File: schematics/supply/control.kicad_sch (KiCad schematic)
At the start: 66 parts, among them J10 USBASP, J11 USBASP, J12 Conn_01x06_Pin, J13 Conn_01x06_Pin, J6 Conn_01x04_Pin, J7 Conn_01x04_Pin, J8 Conn_01x04_Pin, J9 Conn_01x04_Pin, M1 Fan, Q10 IRLML5203, Q4 IRLML0030, Q7 IRLML0030, SW1 EC11W****, SW3 SW_Push, U12 ATmega328-A, U13 ATtiny1616-M, U14 Display_2.2inch_ili9341, U15 LM158DR, X1 HC-49U, 16MHz, X2 CSX-750FCC, 16MHz

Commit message: Found and fixed issues in schematics.
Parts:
- X2: value CSX-750FCC, 16MHz -> 16MHz, SMD3225
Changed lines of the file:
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@@
       (effects (font (size 1.27 1.27)))
     )
-    (property "Value" "CSX-750FCC, 16MHz" (at 213.36 304.8 0)
+    (property "Value" "16MHz, SMD3225" (at 213.36 304.8 0)
       (effects (font (size 1.27 1.27)))
     )

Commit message: Some changes
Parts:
- C21: value 100 nF -> 1 uF
- C26, C29, C35, C36, C37: value 100 nF -> 220 nF
- C36: value 1 uF -> 220 nF
- R30: value 100K -> 10K
- R32: value 200K -> 10K
- R35, R36: value 5K -> 5K1
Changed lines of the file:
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@@
   (symbol (lib_id "Device:C") (at 415.29 389.89 180) (unit 1)
     (in_bom yes) (on_board yes) (dnp no) (fields_autoplaced)
-    (property "Reference" "C36" (at 419.1 389.255 0)
-      (effects (font (size 1.27 1.27)) (justify right))
-    )
-    (property "Value" "1 uF" (at 419.1 391.795 0)
+    (property "Reference" "C36" (at 419.1 388.62 0)
+      (effects (font (size 1.27 1.27)) (justify right))
+    )
+    (property "Value" "220 nF" (at 419.1 391.16 0)
       (effects (font (size 1.27 1.27)) (justify right))
     )
@@
       (effects (font (size 1.27 1.27)))
     )
-    (property "Value" "100 nF" (at 77.47 165.1 90)
+    (property "Value" "220 nF" (at 77.47 165.1 90)
       (effects (font (size 1.27 1.27)))
     )
@@
       (effects (font (size 1.27 1.27) italic) hide)
     )
-    (property "Datasheet" "http://ww1.microchip.com/downloads/en/DeviceDoc/ATtiny3216_ATtiny1616-data-sheet-40001997B.pdf" (at 101.6 331.47 0)
+    (property "Datasheet" "https://static.chipdip.ru/lib/430/DOC011430662.pdf" (at 101.6 331.47 0)
       (effects (font (size 1.27 1.27)) hide)
     )
@@
   (symbol (lib_id "Device:R") (at 208.28 88.9 180) (unit 1)
     (in_bom yes) (on_board yes) (dnp no) (fields_autoplaced)
-    (property "Reference" "R30" (at 210.82 88.265 0)
-      (effects (font (size 1.27 1.27)) (justify right))
-    )
-    (property "Value" "100K" (at 210.82 90.805 0)
+    (property "Reference" "R30" (at 210.82 87.63 0)
+      (effects (font (size 1.27 1.27)) (justify right))
+    )
+    (property "Value" "10K" (at 210.82 90.17 0)
       (effects (font (size 1.27 1.27)) (justify right))
     )
@@
   (symbol (lib_id "Device:C") (at 396.24 369.57 180) (unit 1)
     (in_bom yes) (on_board yes) (dnp no) (fields_autoplaced)
-    (property "Reference" "C36" (at 400.05 368.935 0)
-      (effects (font (size 1.27 1.27)) (justify right))
-    )
-    (property "Value" "1 uF" (at 400.05 371.475 0)
+    (property "Reference" "C36" (at 400.05 368.3 0)
+      (effects (font (size 1.27 1.27)) (justify right))
+    )
+    (property "Value" "220 nF" (at 400.05 370.84 0)
       (effects (font (size 1.27 1.27)) (justify right))
     )
@@
       (effects (font (size 1.27 1.27)) hide)
     )
-    (property "Value" "100 nF" (at 171.45 165.1 90)
+    (property "Value" "220 nF" (at 171.45 165.1 90)
       (effects (font (size 1.27 1.27)))
     )
@@
       (effects (font (size 1.27 1.27)) (justify right))
     )
-    (property "Value" "5K" (at 388.62 370.84 0)
+    (property "Value" "5K1" (at 388.62 370.84 0)
       (effects (font (size 1.27 1.27)) (justify right))
     )
@@
   (symbol (lib_id "Device:C") (at 396.24 294.64 180) (unit 1)
     (in_bom yes) (on_board yes) (dnp no) (fields_autoplaced)
-    (property "Reference" "C36" (at 400.05 294.005 0)
-      (effects (font (size 1.27 1.27)) (justify right))
-    )
-    (property "Value" "1 uF" (at 400.05 296.545 0)
+    (property "Reference" "C36" (at 400.05 293.37 0)
+      (effects (font (size 1.27 1.27)) (justify right))
+    )
+    (property "Value" "220 nF" (at 400.05 295.91 0)
       (effects (font (size 1.27 1.27)) (justify right))
     )
@@
       (effects (font (size 1.27 1.27)))
     )
-    (property "Value" "100 nF" (at 77.47 179.07 90)
+    (property "Value" "220 nF" (at 77.47 179.07 90)
       (effects (font (size 1.27 1.27)))
     )
@@
       (effects (font (size 1.27 1.27)))
     )
-    (property "Value" "100 nF" (at 171.45 191.77 90)
+    (property "Value" "220 nF" (at 171.45 191.77 90)
       (effects (font (size 1.27 1.27)))
     )
@@
       (effects (font (size 1.27 1.27)) (justify right))
     )
-    (property "Value" "200K" (at 262.89 31.75 0)
+    (property "Value" "10K" (at 262.89 31.75 0)
       (effects (font (size 1.27 1.27)) (justify right))
     )
@@
       (effects (font (size 1.27 1.27)))
     )
-    (property "Value" "100 nF" (at 77.47 191.77 90)
+    (property "Value" "220 nF" (at 77.47 191.77 90)
       (effects (font (size 1.27 1.27)))
     )
@@
       (effects (font (size 1.27 1.27)) (justify left))
     )
-    (property "Value" "100 nF" (at 127 295.91 0)
+    (property "Value" "220 nF" (at 127 295.91 0)
       (effects (font (size 1.27 1.27)) (justify left))
     )
@@
       (effects (font (size 1.27 1.27)) (justify left))
     )
-    (property "Value" "100 nF" (at 33.02 52.07 0)
+    (property "Value" "1 uF" (at 33.02 52.07 0)
       (effects (font (size 1.27 1.27)) (justify left))
     )
@@
       (effects (font (size 1.27 1.27)) (justify right))
     )
-    (property "Value" "5K" (at 388.62 295.91 0)
+    (property "Value" "5K1" (at 388.62 295.91 0)
       (effects (font (size 1.27 1.27)) (justify right))
     )
@@
       (effects (font (size 1.27 1.27)) (justify left))
     )
-    (property "Value" "100 nF" (at 121.92 81.28 0)
+    (property "Value" "220 nF" (at 121.92 81.28 0)
       (effects (font (size 1.27 1.27)) (justify left))
     )
@@
       (effects (font (size 1.27 1.27)))
     )
-    (property "Value" "100 nF" (at 171.45 179.07 90)
+    (property "Value" "220 nF" (at 171.45 179.07 90)
       (effects (font (size 1.27 1.27)))
     )
@@
   (symbol (lib_id "Device:C") (at 415.29 314.96 180) (unit 1)
     (in_bom yes) (on_board yes) (dnp no) (fields_autoplaced)
-    (property "Reference" "C36" (at 419.1 314.325 0)
-      (effects (font (size 1.27 1.27)) (justify right))
-    )
-    (property "Value" "1 uF" (at 419.1 316.865 0)
-      (effects (font (size 1.27 1.27)) (justify right))
-    )
+    (property "Reference" "C36" (at 419.1 313.69 0)
+      (effects (font (size 1.27 1.27)) (justify right))
+    )
+    (property "Value" "220 nF" (at 419.1 316.23 0)
+      (effects (font (size 1.27 1.27)) (justify right))
+    )

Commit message: fix pins in firmware
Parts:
- added J23: Conn_01x06_Pin, symbol Connector:Conn_01x06_Pin
- added U22: Display_1.18inch_st7535, symbol My_Library:Display_1.18inch_st7535
- J7, J9, SW1: now fitted; now in the parts list
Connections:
- new net: J23.1 (Pin_1), U22.11 (VCC), U22.2 (RESET)
- new net: J23.2 (Pin_2), U22.3 (DC)
- new net: J23.3 (Pin_3), U22.4 (MOSI)
- new net: J23.4 (Pin_4), U22.5 (SCK)
- new net: J23.6 (Pin_6), U22.1 (CS), U22.10 (GND), U22.9 (GND)
- no-connect marks 9 -> 10

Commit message: supply board - power controllers changed; PWM logic changed
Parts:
- removed C30: 100 nF, Capacitor_SMD:C_0603_1608Metric, symbol Device:C
- removed D14: BAV21WS, Diode_SMD:D_SOD-323F, symbol Device:D
- removed J11: USBASP, Connector_PinHeader_2.54mm:PinHeader_2x05_P2.54mm_Vertical, symbol Connector_Generic:Conn_02x05_Odd_Even
- removed J13: Conn_01x06_Pin, symbol Connector:Conn_01x06_Pin
- removed JP4: Jumper_2_Open, TestPoint:TestPoint_2Pads_Pitch2.54mm_Drill0.8mm, symbol Jumper:Jumper_2_Open
- removed Q10: IRLML5203, Package_TO_SOT_SMD:SOT-23, symbol Transistor_FET:IRLML5203
- removed R37: 10K, Resistor_SMD:R_0805_2012Metric, symbol Device:R
- removed U14: Display_2.2inch_ili9341, symbol My_Library:Display_2.2inch_ili9341
- removed X2: 16MHz, SMD3225, Oscillator:Oscillator_SMD_Abracon_ASE-4Pin_3.2x2.5mm, symbol Oscillator:SG-211
- added C36: 100 nF, Capacitor_SMD:C_0603_1608Metric, symbol Device:C
- added C36: 10 nF, Capacitor_SMD:C_0603_1608Metric, symbol Device:C
- added C41, C43, C47, C51: 1 uF, Capacitor_SMD:C_0603_1608Metric, symbol Device:C
- added D18: BAV21WS, Diode_SMD:D_SOD-323F, symbol Device:D
- added D22: GNL-3012GD, Connector_JST:JST_XH_B2B-XH-A_1x02_P2.50mm_Vertical, symbol Device:LED
- added J12: JST XH B3B, Connector_JST:JST_XH_B3B-XH-A_1x03_P2.50mm_Vertical, symbol Connector:Conn_01x03_Socket
- added J14: Conn_01x03_Pin, symbol Connector:Conn_01x03_Pin
- added J25: Conn_01x05_Socket, Connector_PinHeader_2.54mm:PinHeader_1x05_P2.54mm_Vertical, symbol Connector:Conn_01x05_Socket
- added Q4: IRLML0030, Package_TO_SOT_SMD:SOT-23, symbol Transistor_FET:IRLML0030
- added R35: 10K, Resistor_SMD:R_0805_2012Metric, symbol Device:R
- added R36: 270, Resistor_SMD:R_0805_2012Metric, symbol Device:R
- added R40: 1K, Resistor_SMD:R_0805_2012Metric, symbol Device:R
- added U17: AD9833xRM, Package_SO:MSOP-10_3x3mm_P0.5mm, symbol Interface:AD9833xRM
- added U18: MCP4726A0T-E/CH, Package_TO_SOT_SMD:SOT-23-6, symbol My_Library:MCP4726
- added U19: MAX961, Package_SO:SSOP-8_2.95x2.8mm_P0.65mm, symbol My_Library:MAX961
- added U21: FAN3100, Package_TO_SOT_SMD:SOT-23-5, symbol My_Library:FAN3100
- added X2: ???, Oscillator:Oscillator_SMD_Fordahl_DFAS15-4Pin_5.0x3.2mm_HandSoldering, symbol Oscillator:SG-5032CCN
- SW3: Поле4 (none) -> ON/OFF Button
- renumbered C21 to C28, C22 to C29, C26 to C33, C27 to C34, C28 to C35, C29 to C36, D17 to D15, D18 to D16, D19 to D17, D15 to D19, D16 to D20, J12 to J13, J23 to J15, Q4 to Q3, Q7 to Q6, R28 to R29, R29 to R30, R30 to R31, R31 to R33, R35 to R38, R36 to R39, R38 to R42, R39 to R43, R40 to R44, U12 to U14, U13 to U15, U22 to U16, U15 to U20
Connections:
- net +5V_VSYS: now also C36.2, C41.1, C43.1, C47.1, C51.1, J12.1 (Pin_1), J25.4 (Pin_4), U17.2 (VDD), U18.3 (VDD), U18.6 (VREF), U19.8 (VCC), U21.1 (VCC), X2.1 (OE), X2.4 (Vcc); no longer R33.2, U15.6 (PA5)
- net ATTINY_RXD: now also J25.1 (Pin_1)
- net ATTINY_TXD: now also J25.2 (Pin_2)
- net GND: now also C36.1, C41.2, C43.2, C47.2, C51.2, J25.5 (Pin_5), Q4.2 (S), R35.1, R40.1, U17.4 (DGND), U17.9 (AGND), U18.2 (GND), U19.4 (LATCH_EN), U19.5 (GND), U21.2 (GND), U21.4 (IN-), X2.2 (GND)
- net MISO: no longer J13.5 (Pin_5)
- net MOSI: now also U17.6 (SDATA)
- net POWER_OUTPUT_IC_FB: now also U15.6 (PA5); no longer U15.16 (PC1)
- net SCK: now also U17.7 (SCLK)
- net SCL: now also U18.5 (SCL)
- net SDA: now also U18.4 (SDA)
- net SIGNAL_OUT: now also U21.5 (OUT); no longer U14.14 (PB2)
- net POWER_OUTPUT_VOUT_LED: now reaches U15.18 (PC3)
- net POWER_OUTPUT_VOUT_LED: now also Q4.1 (G), R35.2
- net POWER_OUTPUT_SHUTDOWN#: now reaches U15.9 (PB5)
- net at D13.2 (A): now also D22.2 (A), J14.1 (Pin_1); no longer R33.1
- net at Q3.3 (D): now also R33.1; no longer D13.1 (K)
- net at J15.5 (Pin_5): now also U16.1 (CS)
- net at J15.6 (Pin_6), U16.10 (GND), U16.9 (GND): no longer U16.1 (CS)
- net ATTINY_MISO: no longer names the net of U15.1 (PA2)
- net ATTINY_MOSI: no longer names the net of U15.20 (PA1)
- net ATTINY_SCK: no longer names the net of U15.2 (PA3)
- net ENABLE_POWER_OUTPUT renamed SIGNAL_CS
- net SIGNAL_CS: now also U17.8 (~{FSYNC})
- net POWER_OUTPUT_RESET# renamed ATTINY_RESET#
- net ATTINY_RESET#: now also J25.3 (Pin_3); no longer U14.24 (PC1)
- net RXD: no longer names the net of J10.4 (Pin_4)
- net RXD: no longer U14.30 (PD0)
- new net: U17.5 (MCLK), X2.3 (OUT)
- new net: D22.1 (K), J14.3 (Pin_3)
- new net: J12.2 (Pin_2), R33.2
- new net: J12.3 (Pin_3), R36.2
- new net: U17.10 (VOUT), U19.1 (IN+)
- new net: U18.1 (VOUT), U19.2 (IN-)
- new net: D18.1 (K), R40.2, U19.6 (Q), U21.3 (IN+)
- new net: C36.2, U17.3 (CAP/2.5V)
- new net: C36.1, U17.1 (COMP)
- new net: D13.1 (K), J14.2 (Pin_2)
- new net: Q4.3 (D), R36.1
- new net SIGNAL_ALWAYS_ON: D18.2 (A), U14.24 (PC1)
- new net SIGNAL_GEN_SHTDN: U14.30 (PD0), U19.3 (SHUTDOWN)
- new net TFT_CS: J13.5 (Pin_5), U14.14 (PB2)
- no-connect marks 10 -> 12
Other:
- note added: "I2C address: 0x33"
- note added: "I2C address: 0x60"
- note removed: "ON/OFF button"
- note removed: "vref cap"
- moved on the sheet: D13, D19, D20, J15, Q3, R31, R32, R33, R34, R42, R43, R44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

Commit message: re-design supply board
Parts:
- removed J25: Conn_01x05_Socket, Connector_PinHeader_2.54mm:PinHeader_1x05_P2.54mm_Vertical, symbol Connector:Conn_01x05_Socket
- added C41: 10 nF, Capacitor_SMD:C_0603_1608Metric, symbol Device:C
- added J15: USBASP, Connector_PinHeader_2.54mm:PinHeader_2x05_P2.54mm_Vertical, symbol Connector_Generic:Conn_02x05_Odd_Even
- added R32 (x3): 10K, Resistor_SMD:R_0805_2012Metric, symbol Device:R
- added TP2: IC_FB, TestPoint:TestPoint_Pad_1.0x1.0mm, symbol Connector:TestPoint
- added TP2: PW_SHDN#, TestPoint:TestPoint_Pad_1.0x1.0mm, symbol Connector:TestPoint
- added TP2: SGN_DAC, TestPoint:TestPoint_Pad_1.0x1.0mm, symbol Connector:TestPoint
- added TP2: F_EN, TestPoint:TestPoint_Pad_1.0x1.0mm, symbol Connector:TestPoint
- added TP2: PW_FB, TestPoint:TestPoint_Pad_1.0x1.0mm, symbol Connector:TestPoint
- added TP2: SGN, TestPoint:TestPoint_Pad_1.0x1.0mm, symbol Connector:TestPoint
- added TP2: F_IC, TestPoint:TestPoint_Pad_1.0x1.0mm, symbol Connector:TestPoint
- added TP2: F_R1, TestPoint:TestPoint_Pad_1.0x1.0mm, symbol Connector:TestPoint
- added TP2: PW_CS, TestPoint:TestPoint_Pad_1.0x1.0mm, symbol Connector:TestPoint
- added TP2: BTN_FB, TestPoint:TestPoint_Pad_1.0x1.0mm, symbol Connector:TestPoint
- added TP2: SGN_GEN, TestPoint:TestPoint_Pad_1.0x1.0mm, symbol Connector:TestPoint
- added TP2: PW_VS, TestPoint:TestPoint_Pad_1.0x1.0mm, symbol Connector:TestPoint
- added TP2: F_R2, TestPoint:TestPoint_Pad_1.0x1.0mm, symbol Connector:TestPoint
- renumbered C28 to C26, C29 to C27, C33 to C31, C34 to C32, C35 to C33, C36 to C34, C41 to C38, C43 to C40, C47 to C45, C51 to C49, J6 to J10, J7 to J11, J8 to J12, J9 to J13, J10 to J14, J12 to J16, J13 to J17, J14 to J18, J15 to J19, R40 to R43, R41 to R44, R42 to R45, R43 to R46, R44 to R47
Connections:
- net +5V_VSYS: now also J15.2 (Pin_2), R32.2, R32.2
- net ATTINY_RESET#: now also J15.5 (Pin_5)
- net ATTINY_RXD: now also J15.4 (Pin_4)
- net ATTINY_TXD: now also J15.6 (Pin_6)
- net ENABLE_FAN: now also TP2.1
- net GND: now also C41.2, J15.10 (Pin_10), J15.8 (Pin_8), R32.2
- net IS_ONOFF_BUTTON_PRESSED: now also TP2.1
- net POWER_OUTPUT_CURRENT_SENSE: now also TP2.1
- net POWER_OUTPUT_FB: now also TP2.1
- net POWER_OUTPUT_IC_FB: now also TP2.1
- net POWER_OUTPUT_SHUTDOWN#: now also TP2.1
- net POWER_OUTPUT_VOLT_SENSE: now also TP2.1
- net SIGNAL_ALWAYS_ON: now also R32.1
- net SIGNAL_CS: now also R32.1
- net SIGNAL_GEN_SHTDN: now also R32.1
- net SIGNAL_OUT: now also TP2.1
- net at D15.2 (A), U20.1: now also TP2.1
- net at C36.2, D15.1 (K), D16.1 (K)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: now also TP2.1
- net at D17.2 (A), U20.7: now also TP2.1
- net at U17.10 (VOUT), U19.1 (IN+): now also TP2.1
- net at U18.1 (VOUT), U19.2 (IN-): now also C41.1, TP2.1
- no-connect marks 12 -> 16
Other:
- moved on the sheet: D19, D20

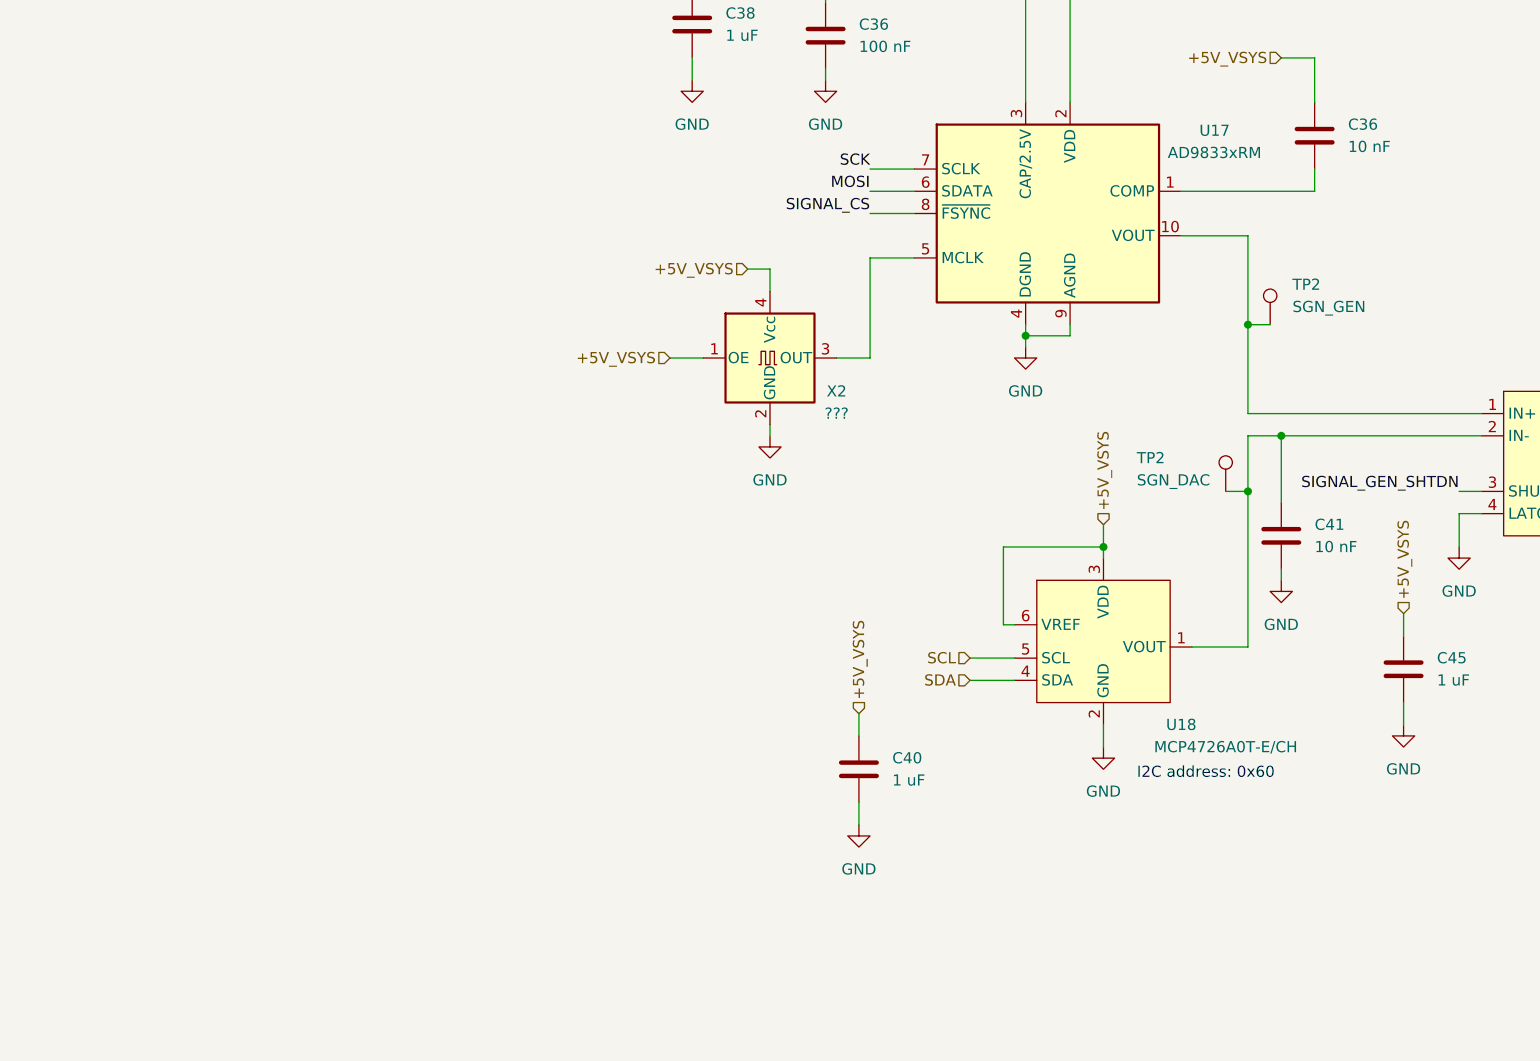
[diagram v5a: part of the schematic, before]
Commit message: Fixed error on board, v1.3 ordered
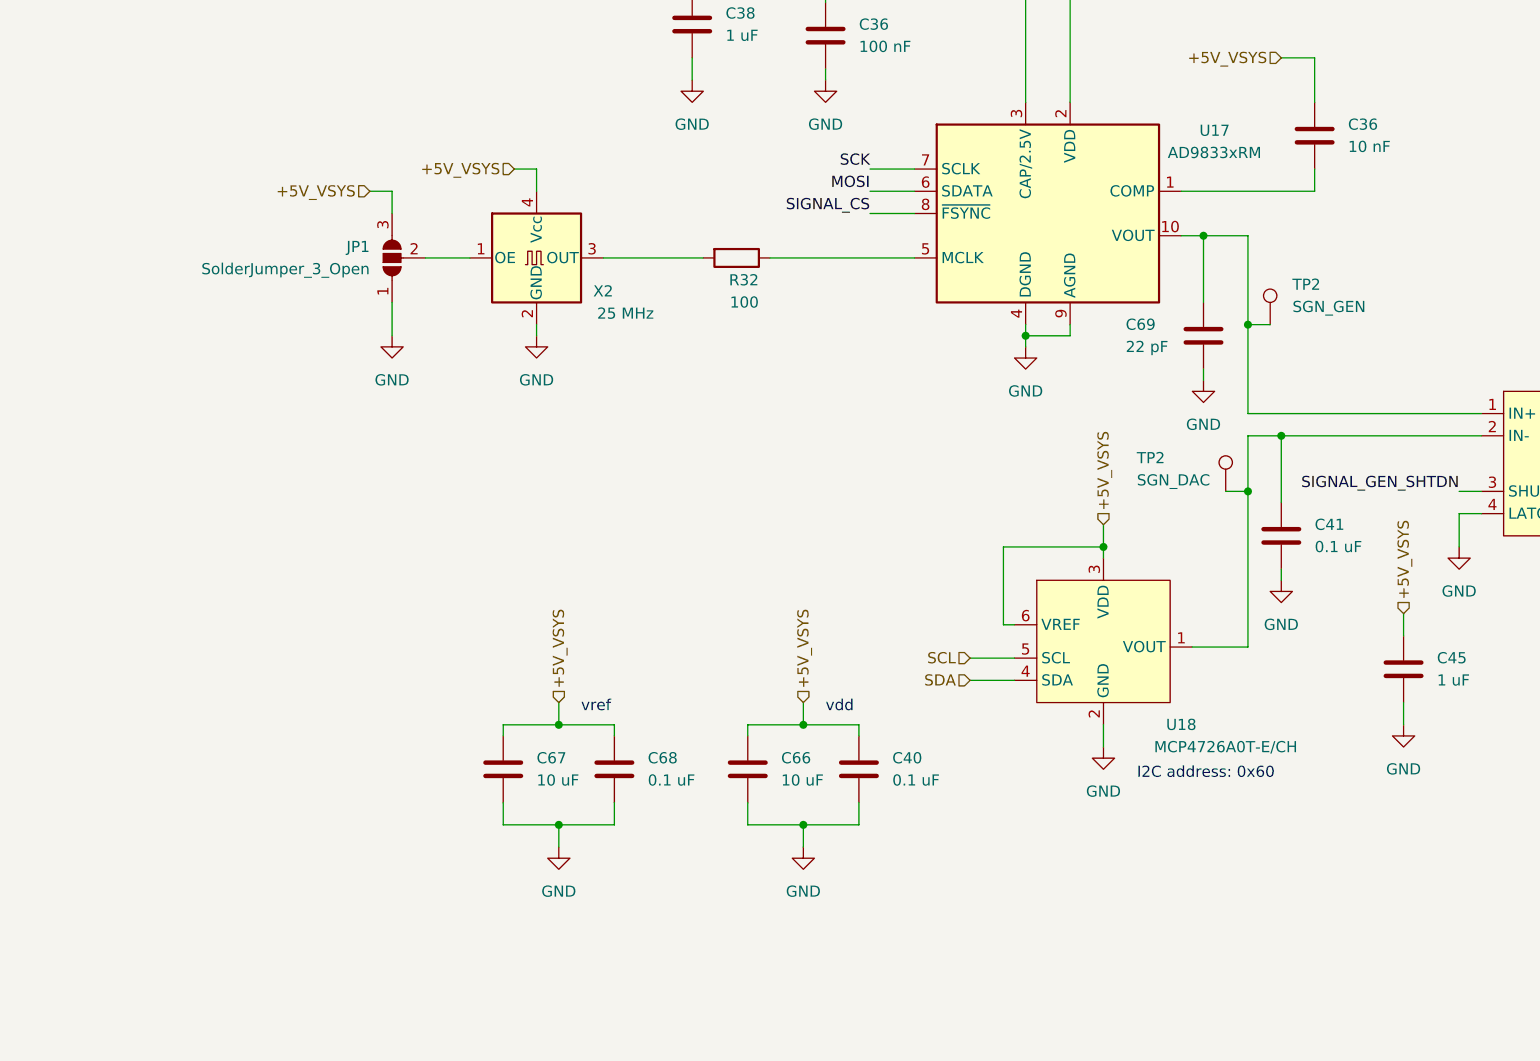
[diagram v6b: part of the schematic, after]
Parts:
- added C66, C67: 10 uF, Capacitor_SMD:C_0603_1608Metric, symbol Device:C
- added C68: 0.1 uF, Capacitor_SMD:C_0603_1608Metric, symbol Device:C
- added C69: 22 pF, Capacitor_SMD:C_0603_1608Metric, symbol Device:C
- added JP1: SolderJumper_3_Open, Jumper:SolderJumper-3_P1.3mm_Open_Pad1.0x1.5mm, symbol Jumper:SolderJumper_3_Open
- added R32: 100, Resistor_SMD:R_0805_2012Metric, symbol Device:R
- C40: value 1 uF -> 0.1 uF
- C41: value 10 nF -> 0.1 uF
- J14, J15: footprint Connector_PinHeader_2.54mm:PinHeader_2x05_P2.54mm_Vertical -> Library:DC3-2x05_p2.54
- U19: footprint Package_SO:SSOP-8_2.95x2.8mm_P0.65mm -> Package_SO:SOP-8_3.76x4.96mm_P1.27mm
- X2: value ??? -> 25 MHz; footprint Oscillator:Oscillator_SMD_Fordahl_DFAS15-4Pin_5.0x3.2mm_HandSoldering -> Oscillator:Oscillator_SMD_EuroQuartz_XO91-4Pin_7.0x5.0mm
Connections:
- net +5V_VSYS: now also C66.1, C67.1, C68.1, JP1.3 (B); no longer X2.1 (OE)
- net GND: now also C66.2, C67.2, C68.2, C69.2, JP1.1 (A)
- net at X2.3 (OUT): now also R32.2; no longer U17.5 (MCLK)
- net at TP2.1, U17.10 (VOUT), U19.1 (IN+): now also C69.1
- new net: JP1.2 (C), X2.1 (OE)
- new net: R32.1, U17.5 (MCLK)
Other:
- note added: "vdd"
- note added: "vref"
- moved on the sheet: X2

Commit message: Continue project
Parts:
- R33, R36: value 270 -> 220
- renumbered D22 to D14, TP2 to TP10, TP2 to TP11, TP2 to TP12, TP2 to TP13, TP2 to TP14, TP2 to TP15, TP2 to TP16, TP2 to TP4, TP2 to TP5, TP2 to TP6, TP2 to TP7, TP2 to TP8, TP2 to TP9
